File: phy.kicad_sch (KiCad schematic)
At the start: 56 parts, among them Q1 BSS138, Q2 BSS138, Q3 BSS138, U2 DP83867IRPAPR

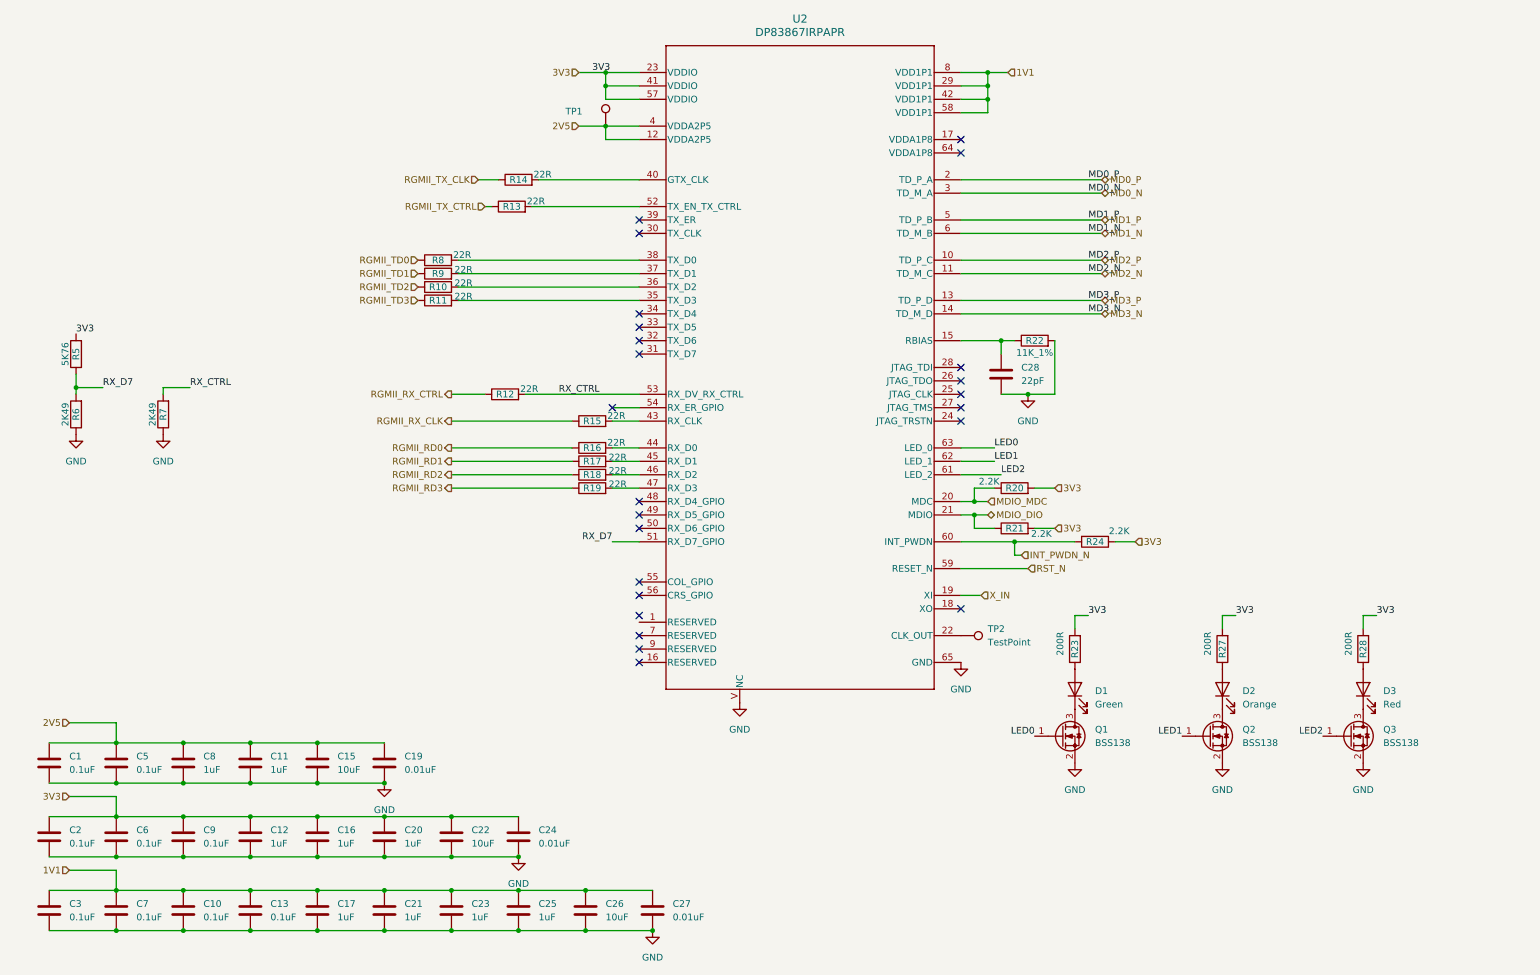
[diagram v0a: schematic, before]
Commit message: Migrate phy sheet to KL library symbols
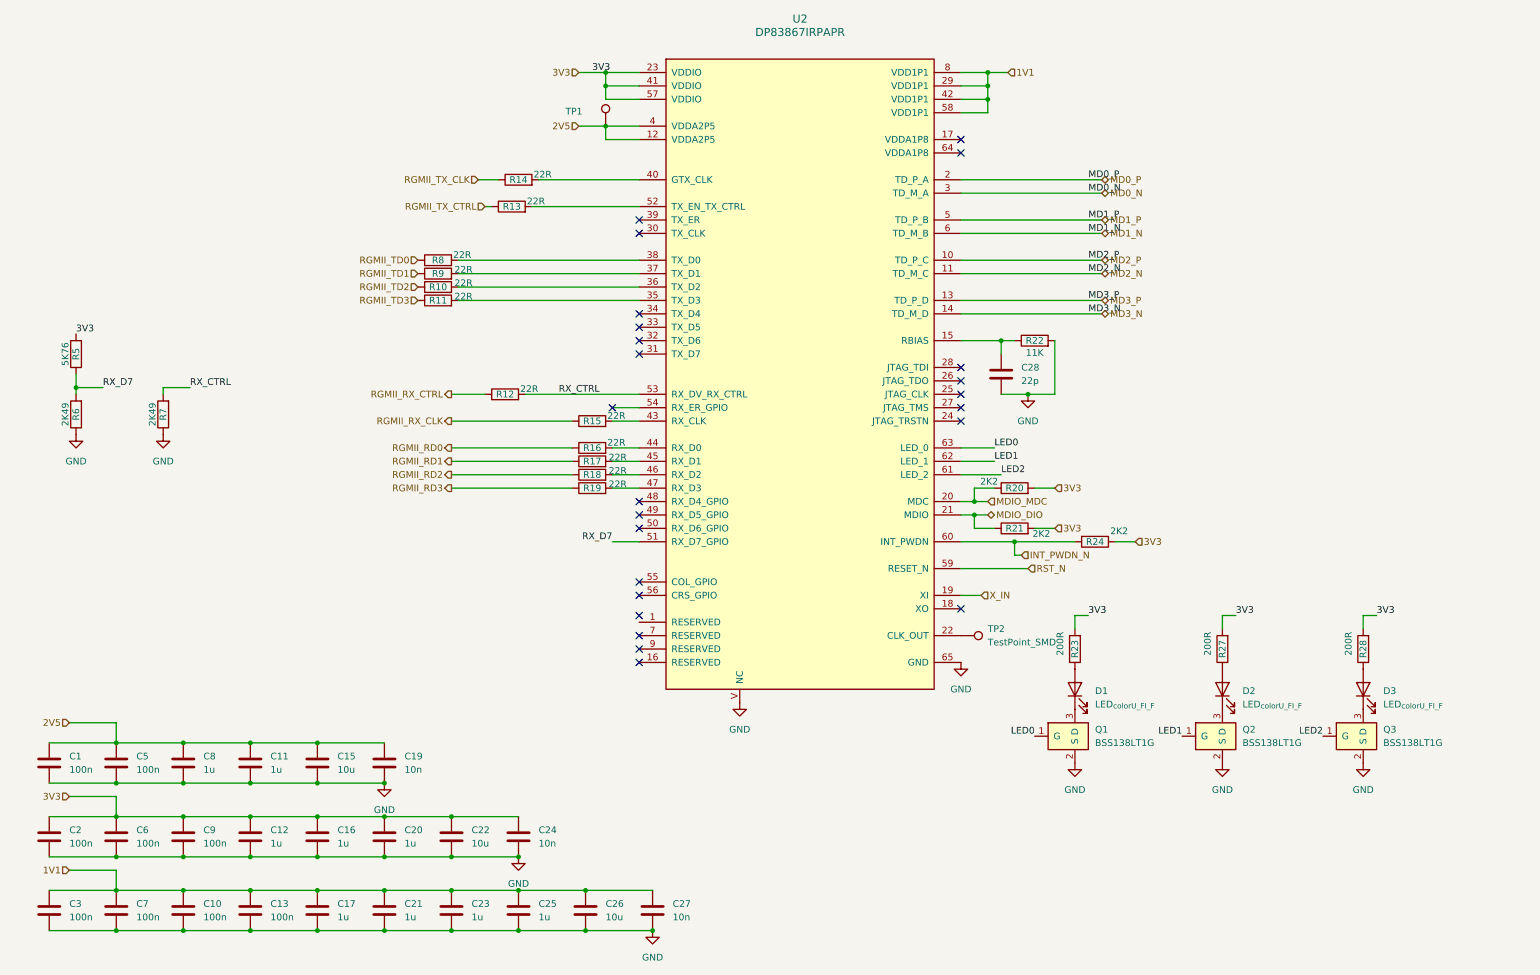
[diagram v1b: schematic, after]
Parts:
- C1, C10, C13, C2, C3, C5, C6, C7, C9: value 0.1uF -> 100n; footprint Capacitor_SMD:C_0402_1005Metric_Pad0.74x0.62mm_HandSolder -> KL_Footprints:C_0402; symbol Device:C -> KL_C:C_100n_35V_10pct_X7R_0402; Dielectric (none) -> X7R; Digikey (none) -> 445-6901-1-ND; LCSC (none) -> C2181802; MPN (none) -> CGA2B3X7R1V104K050BB; Mouser (none) -> 810-CGA2B3X7R1V104K; Package_in_inch (none) -> 0402; Tolerance_in_pct (none) -> 10; Voltage_in_V (none) -> 35
- C11, C12, C16, C17, C20, C21, C23, C25, C8: value 1uF -> 1u; footprint Capacitor_SMD:C_0402_1005Metric_Pad0.74x0.62mm_HandSolder -> KL_Footprints:C_0402; symbol Device:C -> KL_C:C_1u_16V_10pct_X5R_0402; Dielectric (none) -> X5R; Digikey (none) -> TBD; LCSC (none) -> TBD; MPN (none) -> GRM155R61C105KA12D; Mouser (none) -> 81-GRM155R61C105KA12D; Package_in_inch (none) -> 0402; Tolerance_in_pct (none) -> 10; Voltage_in_V (none) -> 16
- C15, C22, C26: value 10uF -> 10u; footprint Capacitor_SMD:C_0402_1005Metric_Pad0.74x0.62mm_HandSolder -> KL_Footprints:C_0402; symbol Device:C -> KL_C:C_10u_6.3V_20pct_X5R_0402; Dielectric (none) -> X5R; Digikey (none) -> TBD; LCSC (none) -> TBD; MPN (none) -> GRM155R60J106ME44D; Mouser (none) -> 81-GRM155R60J106ME44D; Package_in_inch (none) -> 0402; Tolerance_in_pct (none) -> 20; Voltage_in_V (none) -> 6.3
- C19, C24, C27: value 0.01uF -> 10n; footprint Capacitor_SMD:C_0402_1005Metric_Pad0.74x0.62mm_HandSolder -> KL_Footprints:C_0402; symbol Device:C -> KL_C:C_10n_50V_10pct_X7R_0402; Dielectric (none) -> X7R; Digikey (none) -> TBD; LCSC (none) -> TBD; MPN (none) -> GRM155R71H103KA88D; Mouser (none) -> 81-GRM155R71H103KA88D; Package_in_inch (none) -> 0402; Tolerance_in_pct (none) -> 10; Voltage_in_V (none) -> 50
- C28: value 22pF -> 22p; footprint Capacitor_SMD:C_0402_1005Metric_Pad0.74x0.62mm_HandSolder -> KL_Footprints:C_0402; symbol Device:C -> KL_C:C_22p_50V_5pct_C0G_0402; Dielectric (none) -> C0G; Digikey (none) -> TBD; LCSC (none) -> TBD; MPN (none) -> GRM1555C1H220JA01D; Mouser (none) -> 81-GRM1555C1H220JA01D; Package_in_inch (none) -> 0402; Tolerance_in_pct (none) -> 5; Voltage_in_V (none) -> 50
- D1: value Green -> LED_{color}_{U_F}_{I_F}; footprint LED_SMD:LED_0805_2012Metric -> KL_Footprints:LED_0805; symbol Device:LED -> KL_LED:LED_Green_2.1V_0.02A_0805; Color (none) -> Green; Digikey (none) -> TBD; I_F_in_A (none) -> 0.02; LABEL (none) -> ${REFERENCE}:${COLOR}; LCSC (none) -> LTST-C190GKT; MPN (none) -> LTST-C170GKT; Mouser (none) -> 859-LTST-C170GKT; Package_in_inch (none) -> 0805; U_F_in_V (none) -> 2.1; lambda_d_in_nm (none) -> 569
- D2: value Orange -> LED_{color}_{U_F}_{I_F}; footprint LED_SMD:LED_0805_2012Metric -> KL_Footprints:LED_0805; symbol Device:LED -> KL_LED:LED_Orange_2V_0.02A_0805; Color (none) -> Orange; Digikey (none) -> TBD; I_F_in_A (none) -> 0.02; LABEL (none) -> ${REFERENCE}:${COLOR}; LCSC (none) -> C7297440; MPN (none) -> LTST-C170KFKT; Mouser (none) -> 859-LTST-C170KFKT; Package_in_inch (none) -> 0805; U_F_in_V (none) -> 2.0; lambda_d_in_nm (none) -> 605
- D3: value Red -> LED_{color}_{U_F}_{I_F}; footprint LED_SMD:LED_0805_2012Metric -> KL_Footprints:LED_0805; symbol Device:LED -> KL_LED:LED_Red_2V_0.02A_0805; Color (none) -> Red; Digikey (none) -> TBD; I_F_in_A (none) -> 0.02; LABEL (none) -> ${REFERENCE}:${COLOR}; LCSC (none) -> C913101; MPN (none) -> LTST-C170KRKT; Mouser (none) -> 859-LTST-C170KRKT; Package_in_inch (none) -> 0805; U_F_in_V (none) -> 2; lambda_d_in_nm (none) -> 639
- Q1, Q2, Q3: value BSS138 -> BSS138LT1G; footprint Package_TO_SOT_SMD:SOT-23 -> KL_Footprints:SOT-23; symbol Transistor_FET:BSS138 -> KL_Transistor:BSS138LT1G; Digikey (none) -> TBD; I_D_in_A (none) -> 0.22; LCSC (none) -> TBD; MPN (none) -> BSS138LT1G; Mouser (none) -> 863-BSS138LT1G; R_DS_on_in_Ohm (none) -> 3.5; Type (none) -> N-Channel MOSFET; V_DS_in_V (none) -> 50
- R10, R11, R12, R13, R14, R15, R16, R17, R18, R19, R8, R9: footprint Resistor_SMD:R_0402_1005Metric_Pad0.72x0.64mm_HandSolder -> KL_Footprints:R_0402; symbol Device:R -> KL_R:R_22R_0.063W_1pct_0402; Digikey (none) -> TBD; LCSC (none) -> TBD; MPN (none) -> CRCW040222R0FKEDC; Mouser (none) -> 71-CRCW040222R0FKEDC; Package_in_inch (none) -> 0402; Power_in_W (none) -> 0.063; Tolerance_in_pct (none) -> 1
- R20, R21, R24: value 2.2K -> 2K2; footprint Resistor_SMD:R_0402_1005Metric_Pad0.72x0.64mm_HandSolder -> KL_Footprints:R_0402; symbol Device:R -> KL_R:R_2K2_0.063W_1pct_0402; Digikey (none) -> TBD; LCSC (none) -> TBD; MPN (none) -> CRCW04022K20FKEDC; Mouser (none) -> 71-CRCW04022K20FKEDC; Package_in_inch (none) -> 0402; Power_in_W (none) -> 0.063; Tolerance_in_pct (none) -> 1
- R22: value 11K_1% -> 11K; footprint Resistor_SMD:R_0402_1005Metric_Pad0.72x0.64mm_HandSolder -> KL_Footprints:R_0402; symbol Device:R -> KL_R:R_11K_0.063W_1pct_0402; Digikey (none) -> TBD; LCSC (none) -> TBD; MPN (none) -> CRCW040211K0FKEDC; Mouser (none) -> 71-CRCW040211K0FKEDC; Package_in_inch (none) -> 0402; Power_in_W (none) -> 0.063; Tolerance_in_pct (none) -> 1
- R23, R27, R28: footprint Resistor_SMD:R_0402_1005Metric_Pad0.72x0.64mm_HandSolder -> KL_Footprints:R_0402; symbol Device:R -> KL_R:R_200R_0.063W_1pct_0402; Digikey (none) -> TBD; LCSC (none) -> TBD; MPN (none) -> CRCW0402200RFKEDC; Mouser (none) -> 71-CRCW0402200RFKEDC; Package_in_inch (none) -> 0402; Power_in_W (none) -> 0.063; Tolerance_in_pct (none) -> 1
- R5: footprint Resistor_SMD:R_0402_1005Metric_Pad0.72x0.64mm_HandSolder -> KL_Footprints:R_0402; symbol Device:R -> KL_R:R_5K76_0.063W_1pct_0402; Digikey (none) -> TBD; LCSC (none) -> TBD; MPN (none) -> CRCW04025K76FKEDC; Mouser (none) -> 71-CRCW04025K76FKEDC; Package_in_inch (none) -> 0402; Power_in_W (none) -> 0.063; Tolerance_in_pct (none) -> 1
- R6, R7: footprint Resistor_SMD:R_0402_1005Metric_Pad0.72x0.64mm_HandSolder -> KL_Footprints:R_0402; symbol Device:R -> KL_R:R_2K49_0.063W_1pct_0402; Digikey (none) -> TBD; LCSC (none) -> TBD; MPN (none) -> CRCW04022K49FKEDC; Mouser (none) -> 71-CRCW04022K49FKEDC; Package_in_inch (none) -> 0402; Power_in_W (none) -> 0.063; Tolerance_in_pct (none) -> 1
- TP1, TP2: value TestPoint -> TestPoint_SMD; footprint TestPoint:TestPoint_Pad_1.0x1.0mm -> KL_Footprints:TestPoint_SMD_1.0x1.0mm; symbol Connector:TestPoint -> KL_TestPoint:TestPoint_SMD
- U2: footprint PAP0064M_N -> KL_Footprints:HTQFP-64_10x10mm_P0.5mm; symbol DP83867:DP83867IRPAPR -> KL_PHY:DP83867IRPAPR; Digikey (none) -> TBD; I_VDD_A (none) -> TBD; Interface (none) -> RGMII/SGMII; LCSC (none) -> TBD; MPN (none) -> DP83867IRPAPR; Mouser (none) -> 595-DP83867IRPAPR; Speed (none) -> 10/100/1000Base-T

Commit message: Apply signal naming convention to all nets
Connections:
- net 1V1 renamed VDD_1V1
- net 2V5 renamed VDD_2V5
- net 3V3 renamed VDD_3V3
- net INT_PWDN_N renamed INT_PWDN_N_CPU_PHY
- net LED0 renamed LED0_PHY_to_Q1
- net LED1 renamed LED1_PHY_to_Q2
- net LED2 renamed LED2_PHY_to_Q3
- net MD0_N renamed MDI0_PHY_RJ45_N
- net MD0_P renamed MDI0_PHY_RJ45_P
- net MD1_N renamed MDI1_PHY_RJ45_N
- net MD1_P renamed MDI1_PHY_RJ45_P
- net MD2_N renamed MDI2_PHY_RJ45_N
- net MD2_P renamed MDI2_PHY_RJ45_P
- net MD3_N renamed MDI3_PHY_RJ45_N
- net MD3_P renamed MDI3_PHY_RJ45_P
- net MDIO_DIO renamed MDIO_DIO_CPU_PHY
- net MDIO_MDC renamed MDIO_MDC_CPU_PHY
- net RGMII_RD0 renamed RGMII_RD0_PHY_to_CPU
- net RGMII_RD1 renamed RGMII_RD1_PHY_to_CPU
- net RGMII_RD2 renamed RGMII_RD2_PHY_to_CPU
- net RGMII_RD3 renamed RGMII_RD3_PHY_to_CPU
- net RGMII_RX_CLK renamed RGMII_RX_CLK_PHY_to_CPU
- net RGMII_RX_CTRL renamed RGMII_RX_CTRL_PHY_to_CPU
- net RGMII_TD0 renamed RGMII_TD0_CPU_to_PHY
- net RGMII_TD1 renamed RGMII_TD1_CPU_to_PHY
- net RGMII_TD2 renamed RGMII_TD2_CPU_to_PHY
- net RGMII_TD3 renamed RGMII_TD3_CPU_to_PHY
- net RGMII_TX_CLK renamed RGMII_TX_CLK_CPU_to_PHY
- net RGMII_TX_CTRL renamed RGMII_TX_CTRL_CPU_to_PHY
- net RST_N renamed RESET_N_CPU_to_PHY
- net RX_CTRL renamed STRAP_RX_CTRL_PHY
- net RX_D7 renamed STRAP_RX_D7_PHY
- net X_IN renamed CLK_25M_OSC_to_PHY
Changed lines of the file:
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@@
 		)
 	)
-	(label "RX_CTRL"
+	(label "STRAP_RX_CTRL_PHY"
 		(at 118.11 83.82 0)
 		(effects
@@
 		)
 	)
-	(label "MD2_P"
+	(label "MDI2_PHY_RJ45_P"
 		(at 218.44 58.42 0)
 		(effects
@@
 		)
 	)
-	(label "MD2_N"
+	(label "MDI2_PHY_RJ45_N"
 		(at 218.44 60.96 0)
 		(effects
@@
 		)
 	)
-	(label "LED2"
+	(label "LED2_PHY_to_Q3"
 		(at 262.89 148.59 180)
 		(effects
@@
 		)
 	)
-	(label "MD0_P"
+	(label "MDI0_PHY_RJ45_P"
 		(at 218.44 43.18 0)
 		(effects
@@
 		)
 	)
-	(label "LED1"
+	(label "LED1_PHY_to_Q2"
 		(at 236.22 148.59 180)
 		(effects
@@
 		)
 	)
-	(label "MD0_N"
+	(label "MDI0_PHY_RJ45_N"
 		(at 218.44 45.72 0)
 		(effects
@@
 		)
 	)
-	(label "3V3"
+	(label "VDD_3V3"
 		(at 273.05 125.73 0)
 		(effects
@@
 		)
 	)
-	(label "LED0"
+	(label "LED0_PHY_to_Q1"
 		(at 208.28 148.59 180)
 		(effects
@@
 		)
 	)
-	(label "3V3"
+	(label "VDD_3V3"
 		(at 218.44 125.73 0)
 		(effects
@@
 		)
 	)
-	(label "LED0"
+	(label "LED0_PHY_to_Q1"
 		(at 200.66 93.98 0)
 		(effects
@@
 		)
 	)
-	(label "RX_CTRL"
+	(label "STRAP_RX_CTRL_PHY"
 		(at 48.26 82.55 0)
 		(effects
@@
 		)
 	)
-	(label "3V3"
+	(label "VDD_3V3"
 		(at 26.67 72.39 0)
 		(effects
@@
 		)
 	)
-	(label "RX_D7"
+	(label "STRAP_RX_D7_PHY"
 		(at 31.75 82.55 0)
 		(effects
@@
 		)
 	)
-	(label "MD3_N"
+	(label "MDI3_PHY_RJ45_N"
 		(at 218.44 68.58 0)
 		(effects
@@
 		)
 	)
-	(hierarchical_label "X_IN"
+	(hierarchical_label "CLK_25M_OSC_to_PHY"
 		(shape input)
 		(at 198.12 121.92 0)
@@
 		)
 	)
-	(label "LED1"
+	(label "LED1_PHY_to_Q2"
 		(at 200.66 96.52 0)
 		(effects
@@
 		)
 	)
-	(label "LED2"
+	(label "LED2_PHY_to_Q3"
 		(at 201.93 99.06 0)
 		(effects
@@
 		)
 	)
-	(label "MD3_P"
+	(label "MDI3_PHY_RJ45_P"
 		(at 218.44 66.04 0)
 		(effects
@@
 		)
 	)
-	(label "3V3"
+	(label "VDD_3V3"
 		(at 124.46 22.86 0)
 		(effects
@@
 		)
 	)
-	(label "MD1_N"
+	(label "MDI1_PHY_RJ45_N"
 		(at 218.44 53.34 0)
 		(effects
@@
 		)
 	)
-	(label "MD1_P"
+	(label "MDI1_PHY_RJ45_P"
 		(at 218.44 50.8 0)
 		(effects
@@
 		)
 	)
-	(label "RX_D7"
+	(label "STRAP_RX_D7_PHY"
 		(at 128.27 111.76 180)
 		(effects
@@
 		)
 	)
-	(label "3V3"
+	(label "VDD_3V3"
 		(at 246.38 125.73 0)
 		(effects
@@
 		)
 	)
-	(hierarchical_label "MDIO_DIO"
+	(hierarchical_label "MDIO_DIO_CPU_PHY"
 		(shape bidirectional)
 		(at 199.39 106.68 0)
@@
 		)
 	)
-	(hierarchical_label "2V5"
+	(hierarchical_label "VDD_2V5"
 		(shape input)
 		(at 25.4 146.05 180)
@@
 		)
 	)
-	(hierarchical_label "3V3"
+	(hierarchical_label "VDD_3V3"
 		(shape input)
 		(at 121.92 22.86 180)
@@
 		)
 	)
-	(hierarchical_label "2V5"
+	(hierarchical_label "VDD_2V5"
 		(shape input)
 		(at 121.92 33.02 180)
@@
 		)
 	)
-	(hierarchical_label "INT_PWDN_N"
+	(hierarchical_label "INT_PWDN_N_CPU_PHY"
 		(shape input)
 		(at 205.74 114.3 0)
@@
 		)
 	)
-	(hierarchical_label "RGMII_RD3"
+	(hierarchical_label "RGMII_RD3_PHY_to_CPU"
 		(shape output)
 		(at 97.79 101.6 180)
@@
 		)
 	)
-	(hierarchical_label "RST_N"
+	(hierarchical_label "RESET_N_CPU_to_PHY"
 		(shape input)
 		(at 207.01 116.84 0)
@@
 		)
 	)
-	(hierarchical_label "RGMII_RX_CLK"
+	(hierarchical_label "RGMII_RX_CLK_PHY_to_CPU"
 		(shape output)
 		(at 97.79 88.9 180)
@@
 		)
 	)
-	(hierarchical_label "RGMII_RD0"
+	(hierarchical_label "RGMII_RD0_PHY_to_CPU"
 		(shape output)
 		(at 97.79 93.98 180)
@@
 		)
 	)
-	(hierarchical_label "RGMII_TX_CLK"
+	(hierarchical_label "RGMII_TX_CLK_CPU_to_PHY"
 		(shape input)
 		(at 102.87 43.18 180)
@@
 		)
 	)
-	(hierarchical_label "3V3"
+	(hierarchical_label "VDD_3V3"
 		(shape input)
 		(at 25.4 160.02 180)
@@
 		)
 	)
-	(hierarchical_label "RGMII_RD2"
+	(hierarchical_label "RGMII_RD2_PHY_to_CPU"
 		(shape output)
 		(at 97.79 99.06 180)
@@
 		)
 	)
-	(hierarchical_label "RGMII_TD0"
+	(hierarchical_label "RGMII_TD0_CPU_to_PHY"
 		(shape input)
 		(at 91.44 58.42 180)
@@
 		)
 	)
-	(hierarchical_label "MDIO_MDC"
+	(hierarchical_label "MDIO_MDC_CPU_PHY"
 		(shape input)
 		(at 199.39 104.14 0)
@@
 		)
 	)
-	(hierarchical_label "1V1"
+	(hierarchical_label "VDD_1V1"
 		(shape input)
 		(at 203.2 22.86 0)
@@
 		)
 	)
-	(hierarchical_label "RGMII_TX_CTRL"
+	(hierarchical_label "RGMII_TX_CTRL_CPU_to_PHY"
 		(shape input)
 		(at 104.14 48.26 180)
@@
 		)
 	)
-	(hierarchical_label "3V3"
+	(hierarchical_label "VDD_3V3"
 		(shape input)
 		(at 212.09 101.6 0)
@@
 		)
 	)
-	(hierarchical_label "RGMII_TD2"
+	(hierarchical_label "RGMII_TD2_CPU_to_PHY"
 		(shape input)
 		(at 91.44 63.5 180)
@@
 		)
 	)
-	(hierarchical_label "RGMII_RX_CTRL"
+	(hierarchical_label "RGMII_RX_CTRL_PHY_to_CPU"
 		(shape output)
 		(at 97.79 83.82 180)
@@
 		)
 	)
-	(hierarchical_label "RGMII_TD1"
+	(hierarchical_label "RGMII_TD1_CPU_to_PHY"
 		(shape input)
 		(at 91.44 60.96 180)
@@
 		)
 	)
-	(hierarchical_label "RGMII_RD1"
+	(hierarchical_label "RGMII_RD1_PHY_to_CPU"
 		(shape output)
 		(at 97.79 96.52 180)
@@
 		)
 	)
-	(hierarchical_label "3V3"
+	(hierarchical_label "VDD_3V3"
 		(shape input)
 		(at 227.33 111.76 0)
@@
 		)
 	)
-	(hierarchical_label "1V1"
+	(hierarchical_label "VDD_1V1"
 		(shape input)
 		(at 25.4 173.99 180)
@@
 		)
 	)
-	(hierarchical_label "3V3"
+	(hierarchical_label "VDD_3V3"
 		(shape input)
 		(at 212.09 109.22 0)
@@
 		)
 	)
-	(hierarchical_label "RGMII_TD3"
+	(hierarchical_label "RGMII_TD3_CPU_to_PHY"
 		(shape input)
 		(at 91.44 66.04 180)
@@
 		)
 	)
-	(hierarchical_label "MD0_P"
+	(hierarchical_label "MDI0_PHY_RJ45_P"
 		(shape bidirectional)
 		(at 220.98 43.18 0)
@@
 		)
 	)
-	(hierarchical_label "MD0_N"
+	(hierarchical_label "MDI0_PHY_RJ45_N"
 		(shape bidirectional)
 		(at 220.98 45.72 0)
@@
 		)
 	)
-	(hierarchical_label "MD1_P"
+	(hierarchical_label "MDI1_PHY_RJ45_P"
 		(shape bidirectional)
 		(at 220.98 50.8 0)
@@
 		)
 	)
-	(hierarchical_label "MD1_N"
+	(hierarchical_label "MDI1_PHY_RJ45_N"
 		(shape bidirectional)
 		(at 220.98 53.34 0)
@@
 		)
 	)
-	(hierarchical_label "MD2_P"
+	(hierarchical_label "MDI2_PHY_RJ45_P"
 		(shape bidirectional)
 		(at 220.98 58.42 0)
@@
 		)
 	)
-	(hierarchical_label "MD2_N"
+	(hierarchical_label "MDI2_PHY_RJ45_N"
 		(shape bidirectional)
 		(at 220.98 60.96 0)
@@
 		)
 	)
-	(hierarchical_label "MD3_P"
+	(hierarchical_label "MDI3_PHY_RJ45_P"
 		(shape bidirectional)
 		(at 220.98 66.04 0)
@@
 		)
 	)
-	(hierarchical_label "MD3_N"
+	(hierarchical_label "MDI3_PHY_RJ45_N"
 		(shape bidirectional)
 		(at 220.98 68.58 0)
